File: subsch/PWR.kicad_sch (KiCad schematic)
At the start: 3 parts

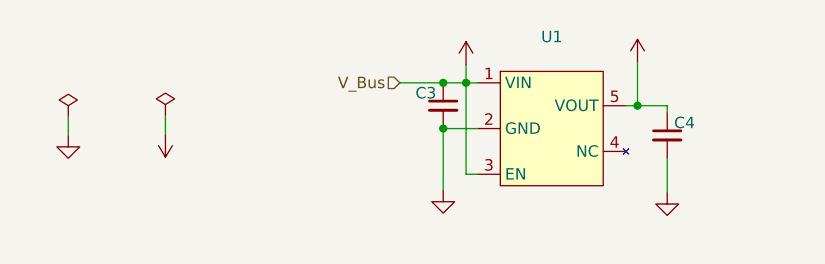
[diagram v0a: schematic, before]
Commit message: Add ESD protection
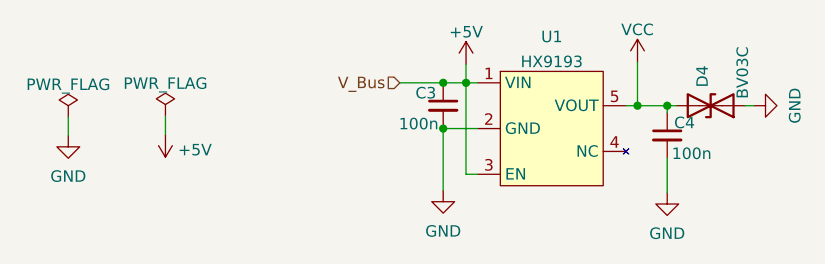
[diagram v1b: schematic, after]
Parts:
- added D4: BV03C, Diode_SMD:D_SOD-323, symbol Device:D_TVS
- C3, C4: value (none) -> 100n; footprint (none) -> Capacitor_SMD:C_0603_1608Metric
- U1: value (none) -> HX9193; footprint (none) -> Package_TO_SOT_SMD:SOT-23-5_HandSoldering
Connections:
- net GND: now also D4.1 (A1)
- net VCC: now also D4.2 (A2)
